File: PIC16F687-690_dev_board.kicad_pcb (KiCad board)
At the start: 2 copper layers, 6 parts, among them J1 Conn_01x06_Pin, U1 PIC16F690-IP

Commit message: finalized layout organization
finalized layout organization
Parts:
- added J2: Conn_01x20_Pin, Connector_PinHeader_2.54mm:PinHeader_1x20_P2.54mm_Vertical, F.Cu at (147.8, 61.5)
- moved C1 31.4 mm to (129.1, 69.6)
- moved R1 26.7 mm to (122.9, 70.4), turned to -90 degrees
- moved J1 19.2 mm to (122.9, 64.0), turned to 90 degrees
- moved D1 12.2 mm to (142.5, 69.1), turned to 180 degrees
- moved R2 9.48 mm to (140.2, 87.6), turned to 90 degrees
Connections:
- U1 pad 10: unconnected-(U1-TX/CK/RB7-Pad10) -> Net-(J2-Pin_17)
- U1 pad 11: unconnected-(U1-SCK/SCL/RB6-Pad11) -> Net-(J2-Pin_18)
- U1 pad 12: unconnected-(U1-RX/DT/AN11/RB5-Pad12) -> Net-(J2-Pin_19)
- U1 pad 13: unconnected-(U1-SDI/SDA/AN10/RB4-Pad13) -> Net-(J2-Pin_20)
- U1 pad 14: unconnected-(U1-RC2/AN6/C12IN2-/P1D-Pad14) -> Net-(J2-Pin_5)
- U1 pad 15: unconnected-(U1-RC1/AN5/C12IN1--Pad15) -> Net-(J2-Pin_4)
- U1 pad 17: unconnected-(U1-C1OUT/T0CKI/INT/AN2/RA2-Pad17) -> Net-(J2-Pin_13)
- U1 pad 2: unconnected-(U1-T1CKI/OSC1/CLKIN/RA5-Pad2) -> Net-(J2-Pin_16)
- U1 pad 3: unconnected-(U1-~{T1G}/OSC2/CLKOUT/AN3/RA4-Pad3) -> Net-(J2-Pin_15)
- U1 pad 5: unconnected-(U1-RC5/CCP1/P1A-Pad5) -> Net-(J2-Pin_8)
- U1 pad 6: unconnected-(U1-RC4/C2OUT/P1B-Pad6) -> Net-(J2-Pin_7)
- U1 pad 7: unconnected-(U1-RC3/AN7/C12IN3-/P1C-Pad7) -> Net-(J2-Pin_6)
- U1 pad 8: unconnected-(U1-RC6/AN8/~{SS}-Pad8) -> Net-(J2-Pin_9)
- U1 pad 9: unconnected-(U1-RC7/AN9/SDO-Pad9) -> Net-(J2-Pin_10)
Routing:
- net MCLR: track 0.00 -> 54.6 mm
- net Net-(J2-Pin_16): track 0.00 -> 42.0 mm, vias 0 -> 1
- net VCC: track 0.00 -> 40.5 mm
- net Net-(J2-Pin_3): track 0.00 -> 36.1 mm
- net PGC5: track 0.00 -> 35.3 mm, vias 0 -> 2
- net Net-(J2-Pin_15): track 0.00 -> 35.1 mm, vias 0 -> 2
- net PGD4: track 0.00 -> 33.4 mm, vias 0 -> 1
- net Net-(J2-Pin_20): track 0.00 -> 31.0 mm
- net Net-(J2-Pin_6): track 0.00 -> 30.7 mm, vias 0 -> 2
- net Net-(J2-Pin_9): track 0.00 -> 29.7 mm
- net Net-(J2-Pin_8): track 0.00 -> 29.6 mm, vias 0 -> 2
- net Net-(J2-Pin_10): track 0.00 -> 29.4 mm
- net Net-(J2-Pin_7): track 0.00 -> 24.4 mm, vias 0 -> 2
- net Net-(J2-Pin_19): track 0.00 -> 24.0 mm
- net Net-(J2-Pin_4): track 0.00 -> 22.8 mm, vias 0 -> 1
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- added copper zone on B.Cu, net GND
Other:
- board outline added: 29.5 x 52.3 mm

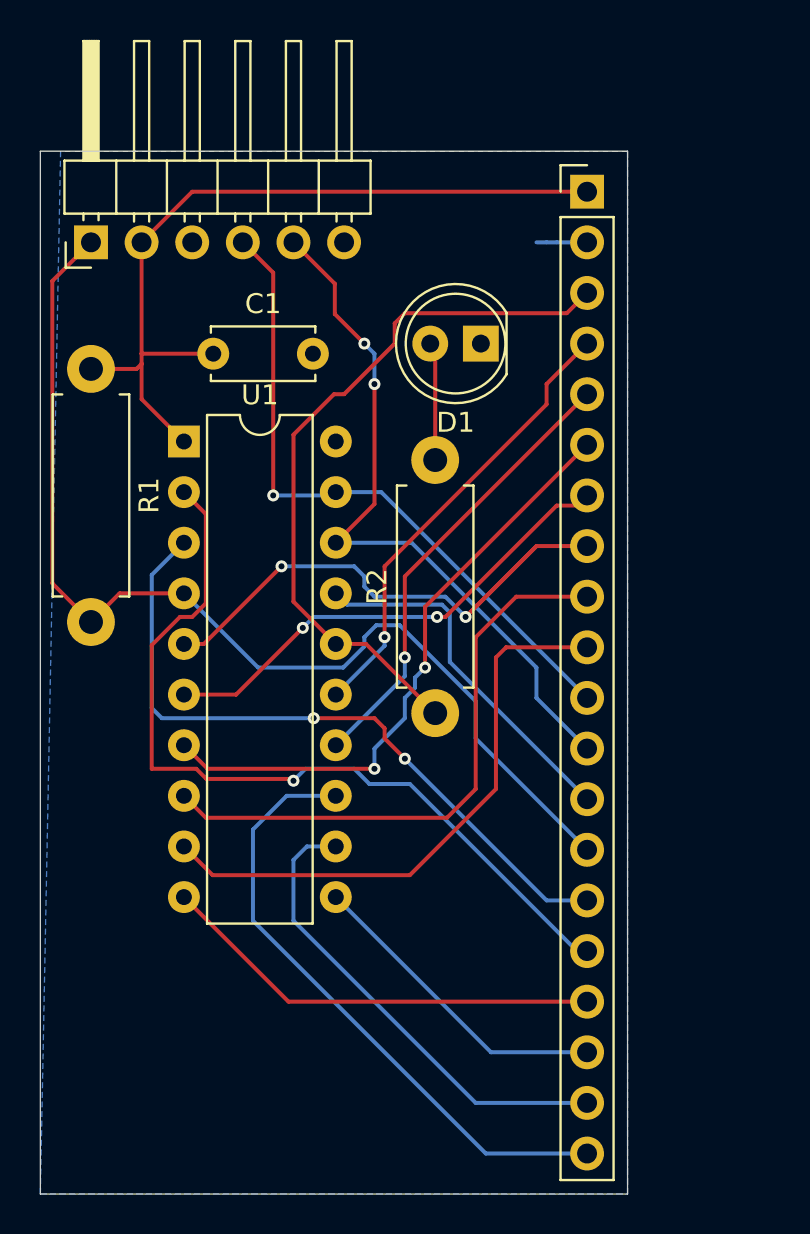
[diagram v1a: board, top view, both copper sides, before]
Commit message: finished silkscreen
finished silkscreen and sent into production at JLCPCB
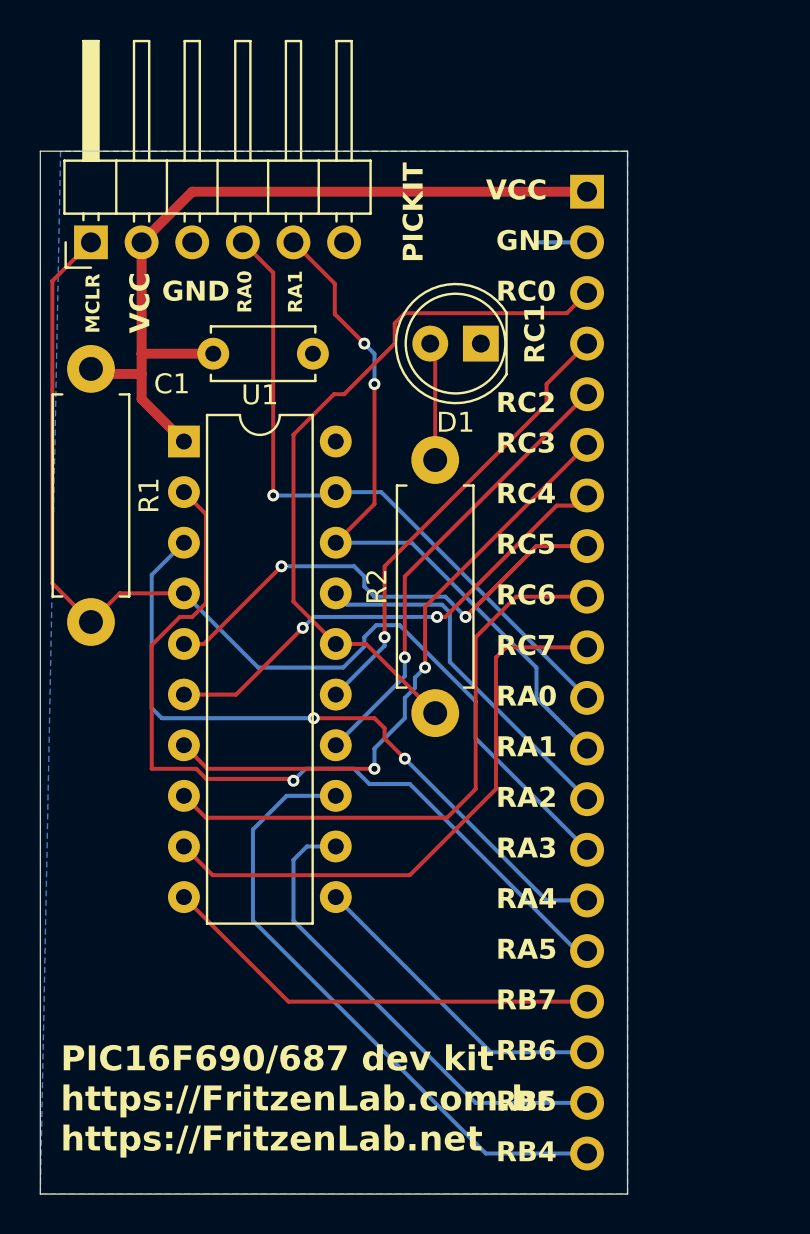
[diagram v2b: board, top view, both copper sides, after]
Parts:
- J2: moved to B.Cu
- turned J2 to 180 degrees
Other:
- board text added: "GND"
- board text added: "MCLR"
- board text added: "PIC16F690/687 dev kit https://FritzenLab.com.br https://FritzenLab.net"
- board text added: "PICKIT"
- board text added: "RA0"
- board text added: "RA1"
- board text added: "RA2"
- board text added: "RA3"
- board text added: "RA4"
- board text added: "RA5"
- board text added: "RB4"
- board text added: "RB5"
- board text added: "RB6"
- board text added: "RB7"
- board text added: "RC0"
- board text added: "RC1"
- board text added: "RC2"
- board text added: "RC3"
- board text added: "RC4"
- board text added: "RC5"
- board text added: "RC6"
- board text added: "RC7"
- board text added: "VCC"
